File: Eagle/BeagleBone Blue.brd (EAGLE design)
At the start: 86.4 x 54.6 mm, 125 parts, among them M1 JST_ZH_2, M2 JST_ZH_2, M3 JST_ZH_2, M4 JST_ZH_2, Q3 MOSFET-N, Q4 MOSFET-P

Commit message: move Hbridges to back
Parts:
- moved H2 9.46 mm to (81.5, 24.1), flipped to the bottom, turned to 270 degrees
- moved H1 2.01 mm to (74.4, 13.6), flipped to the bottom, turned to 270 degrees
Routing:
- net MOT1B: track 12.2 -> 0.65 mm
- net MOT1A: track 9.95 -> 0.65 mm, vias 1 -> 0
- net MOT2A: track 7.24 -> 0.65 mm
- net MOT2B: track 6.79 -> 0.65 mm
- net GND: track 82.4 -> 81.7 mm

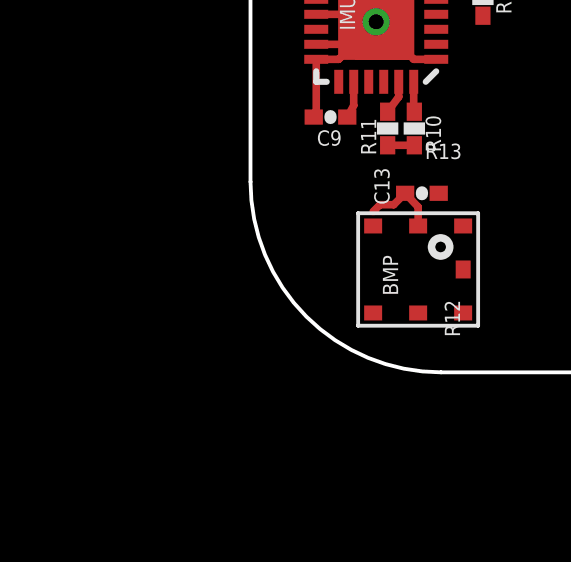
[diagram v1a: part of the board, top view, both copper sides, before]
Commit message: added MPU-9250 component
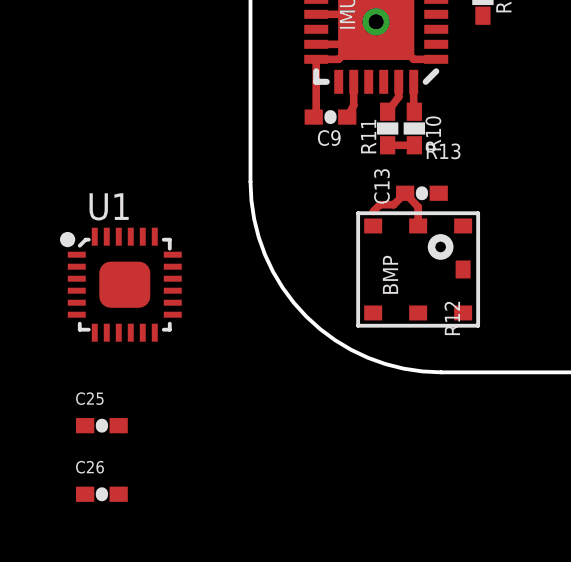
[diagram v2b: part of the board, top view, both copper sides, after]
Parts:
- added C25, C26: 0.1uF, Strawson_Eagle_Lib:0402-CAP
- added U1: MPU-9250, Strawson_Eagle_Lib:QFN24G-0.4-3X3MM
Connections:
- new net N$70: C26.2, U1.10
- net 3.3V: now also C25.1, U1.1, U1.13, U1.8
- net GND: now also C25.2, C26.1, U1.18, U1.20, U1.25, U1.9
- net I2C2_SCL: now also U1.23
- net I2C2_SDA: now also U1.24
- net IMU_INT: now also U1.12
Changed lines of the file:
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@@
 <layer number="56" name="wert" color="7" fill="1" visible="yes" active="yes"/>
 <layer number="57" name="tCAD" color="7" fill="1" visible="no" active="no"/>
+<layer number="90" name="Modules" color="5" fill="1" visible="no" active="no"/>
 <layer number="91" name="Nets" color="2" fill="1" visible="no" active="no"/>
 <layer number="92" name="Busses" color="1" fill="1" visible="no" active="no"/>
@@
 </element>
 <element name="U$7" library="Strawson_Eagle_Lib" package="BEAGLEBONE_BLUE_NO_HOLES" value="" x="0" y="54.61" rot="R270"/>
+<element name="U1" library="Strawson_Eagle_Lib" package="QFN24G-0.4-3X3MM" value="MPU-9250" x="-4.191" y="2.921">
+<attribute name="MPN" value="MPU-9250" x="-4.191" y="2.921" size="1.778" layer="27" display="off"/>
+</element>
+<element name="C25" library="Strawson_Eagle_Lib" package="0402-CAP" value="0.1uF" x="-4.953" y="-1.778"/>
+<element name="C26" library="Strawson_Eagle_Lib" package="0402-CAP" value="0.1uF" x="-4.953" y="-4.064"/>
 </elements>
 <signals>
@@
 <wire x1="4.941" y1="9.684" x2="4.941" y2="9.1828" width="0.254" layer="1"/>
 <wire x1="4.941" y1="9.1828" x2="4.572" y2="8.6868" width="0.254" layer="1"/>
+<contactref element="U1" pad="23"/>
 <wire x1="5.588" y1="1.979" x2="4.572" y2="8.6868" width="0" layer="19" extent="1-1"/>
+<wire x1="-4.791" y1="4.521" x2="4.572" y2="8.6868" width="0" layer="19" extent="1-1"/>
 </signal>
 <signal name="I2C2_SDA">
@@
 <wire x1="5.441" y1="9.684" x2="5.441" y2="8.7068" width="0.254" layer="1"/>
 <wire x1="5.441" y1="8.7068" x2="5.461" y2="8.6868" width="0.254" layer="1"/>
+<contactref element="U1" pad="24"/>
 <wire x1="7.088" y1="1.979" x2="5.461" y2="8.6868" width="0" layer="19" extent="1-1"/>
+<wire x1="-5.191" y1="4.521" x2="5.441" y2="8.7068" width="0" layer="19" extent="1-1"/>
 </signal>
 <signal name="PWM_2B">
@@
 <wire x1="4.7752" y1="5.588" x2="5.1562" y2="5.969" width="0.254" layer="1"/>
 <wire x1="77.0382" y1="41.783" x2="77.0382" y2="40.767" width="0.254" layer="1"/>
-<wire x1="77.0382" y1="41.783" x2="83.28" y2="42.672" width="0" layer="19" extent="1-1"/>
-<wire x1="76.7842" y1="37.084" x2="77.0382" y2="40.767" width="0" layer="19" extent="1-1"/>
-<wire x1="76.7842" y1="36.195" x2="76.7842" y2="37.084" width="0" layer="19" extent="1-1"/>
-<wire x1="77.6478" y1="32.512" x2="76.7842" y2="36.195" width="0" layer="19" extent="1-1"/>
+<contactref element="U1" pad="8"/>
+<contactref element="U1" pad="1"/>
+<contactref element="C25" pad="1"/>
+<contactref element="U1" pad="13"/>
+<wire x1="83.28" y1="37.719" x2="83.28" y2="42.672" width="0" layer="19" extent="1-1"/>
+<wire x1="83.28" y1="32.766" x2="83.28" y2="37.719" width="0" layer="19" extent="1-1"/>
+<wire x1="83.28" y1="27.94" x2="83.28" y2="32.766" width="0" layer="19" extent="1-1"/>
+<wire x1="77.6478" y1="32.512" x2="83.28" y2="32.766" width="0" layer="19" extent="1-1"/>
 <wire x1="76.5302" y1="31.623" x2="77.6478" y2="32.512" width="0" layer="19" extent="1-1"/>
 <wire x1="76.0222" y1="29.21" x2="76.5302" y2="31.623" width="0" layer="19" extent="1-1"/>
 <wire x1="76.0222" y1="28.194" x2="76.0222" y2="29.21" width="0" layer="19" extent="1-1"/>
-<wire x1="83.28" y1="32.766" x2="77.6478" y2="32.512" width="0" layer="19" extent="1-1"/>
-<wire x1="83.28" y1="27.94" x2="83.28" y2="32.766" width="0" layer="19" extent="1-1"/>
-<wire x1="83.28" y1="37.719" x2="83.28" y2="32.766" width="0" layer="19" extent="1-1"/>
-<wire x1="77.878" y1="25.105" x2="76.0222" y2="28.194" width="0" layer="19" extent="1-1"/>
-<wire x1="64.389" y1="18.4658" x2="77.878" y2="25.105" width="0" layer="19" extent="1-1"/>
-<wire x1="70.766" y1="14.564" x2="64.389" y2="18.4658" width="0" layer="19" extent="1-1"/>
-<wire x1="71.247" y1="4.794" x2="70.766" y2="14.564" width="0" layer="19" extent="1-1"/>
+<wire x1="77.878" y1="25.105" x2="76.0222" y2="28.194" width="0" layer="19" extent="1-16"/>
+<wire x1="76.7842" y1="36.195" x2="77.6478" y2="32.512" width="0" layer="19" extent="1-1"/>
+<wire x1="76.7842" y1="37.084" x2="76.7842" y2="36.195" width="0" layer="19" extent="1-1"/>
+<wire x1="77.0382" y1="40.767" x2="76.7842" y2="37.084" width="0" layer="19" extent="1-1"/>
+<wire x1="70.766" y1="14.564" x2="77.878" y2="25.105" width="0" layer="19" extent="16-16"/>
+<wire x1="64.389" y1="18.4658" x2="70.766" y2="14.564" width="0" layer="19" extent="1-16"/>
+<wire x1="71.247" y1="4.794" x2="70.766" y2="14.564" width="0" layer="19" extent="1-16"/>
 <wire x1="64.897" y1="4.921" x2="71.247" y2="4.794" width="0" layer="19" extent="1-1"/>
 <wire x1="53.721" y1="6.413" x2="64.897" y2="4.921" width="0" layer="19" extent="1-1"/>
@@
 <wire x1="28.829" y1="10.0838" x2="34.544" y2="9.9568" width="0" layer="19" extent="1-1"/>
 <wire x1="21.855" y1="6.604" x2="28.829" y2="10.0838" width="0" layer="19" extent="1-1"/>
-<wire x1="5.588" y1="4.879" x2="21.855" y2="6.604" width="0" layer="19" extent="1-1"/>
+<wire x1="5.588" y1="5.5118" x2="21.855" y2="6.604" width="0" layer="19" extent="1-1"/>
 <wire x1="4.088" y1="4.879" x2="4.088" y2="5.358" width="0" layer="19" extent="1-1"/>
 <wire x1="5.461" y1="7.5692" x2="5.1562" y2="5.969" width="0" layer="19" extent="1-1"/>
@@
 <wire x1="6.4008" y1="15.113" x2="4.941" y2="13.684" width="0" layer="19" extent="1-1"/>
 <wire x1="2.191" y1="12.934" x2="4.941" y2="13.684" width="0" layer="19" extent="1-1"/>
+<wire x1="-2.591" y1="1.921" x2="4.088" y2="4.879" width="0" layer="19" extent="1-1"/>
+<wire x1="-4.791" y1="1.321" x2="-2.591" y2="1.921" width="0" layer="19" extent="1-1"/>
+<wire x1="-5.791" y1="3.921" x2="-4.791" y2="1.321" width="0" layer="19" extent="1-1"/>
+<wire x1="-5.5118" y1="-1.778" x2="-4.791" y2="1.321" width="0" layer="19" extent="1-1"/>
 </signal>
 <signal name="N$57">
@@
 <signal name="IMU_INT">
 <contactref element="IMU" pad="12"/>
+<contactref element="U1" pad="12"/>
+<wire x1="-3.191" y1="1.321" x2="2.941" y2="13.684" width="0" layer="19" extent="1-1"/>
 </signal>
 <signal name="QEP_0B">
@@
 <wire x1="46.99" y1="40.132" x2="51.308" y2="40.132" width="0.254" layer="16"/>
 <wire x1="51.308" y1="40.132" x2="51.308" y2="46.101" width="0.254" layer="16"/>
+<contactref element="U1" pad="25"/>
+<contactref element="U1" pad="20"/>
+<contactref element="U1" pad="9"/>
+<contactref element="C25" pad="2"/>
+<contactref element="U1" pad="18"/>
+<contactref element="C26" pad="1"/>
 <wire x1="84.28" y1="37.719" x2="84.28" y2="42.672" width="0" layer="19" extent="1-1"/>
 <wire x1="84.28" y1="32.766" x2="84.28" y2="37.719" width="0" layer="19" extent="1-1"/>
@@
 <wire x1="78.078" y1="11.964" x2="78.078" y2="15.214" width="0" layer="19" extent="16-16"/>
 <wire x1="78.078" y1="11.314" x2="78.078" y2="11.964" width="0" layer="19" extent="16-16"/>
-<wire x1="64.389" y1="17.3482" x2="78.078" y2="15.214" width="0" layer="19" extent="1-16"/>
-<wire x1="70.766" y1="13.264" x2="64.389" y2="17.3482" width="0" layer="19" extent="1-16"/>
-<wire x1="62.738" y1="19.7358" x2="64.389" y2="17.3482" width="0" layer="19" extent="1-1"/>
-<wire x1="71.247" y1="5.794" x2="78.078" y2="11.314" width="0" layer="19" extent="1-16"/>
+<wire x1="70.766" y1="13.264" x2="78.078" y2="11.964" width="0" layer="19" extent="16-16"/>
+<wire x1="71.247" y1="5.794" x2="70.766" y2="13.264" width="0" layer="19" extent="1-16"/>
 <wire x1="64.897" y1="5.921" x2="71.247" y2="5.794" width="0" layer="19" extent="1-1"/>
 <wire x1="58.801" y1="7.413" x2="64.897" y2="5.921" width="0" layer="19" extent="1-1"/>
@@
 <wire x1="30.861" y1="6.175" x2="35.433" y2="6.175" width="0" layer="19" extent="1-1"/>
 <wire x1="30.861" y1="5.175" x2="30.861" y2="6.175" width="0" layer="19" extent="1-1"/>
+<wire x1="64.389" y1="17.3482" x2="70.766" y2="13.264" width="0" layer="19" extent="1-16"/>
+<wire x1="62.738" y1="19.7358" x2="64.389" y2="17.3482" width="0" layer="19" extent="1-1"/>
 <wire x1="63.119" y1="29.197" x2="62.738" y2="19.7358" width="0" layer="19" extent="1-1"/>
 <wire x1="61.087" y1="32.9565" x2="63.119" y2="29.197" width="0" layer="19" extent="1-1"/>
@@
 <wire x1="6.2738" y1="5.969" x2="6.191" y2="10.434" width="0" layer="19" extent="1-1"/>
 <wire x1="7.088" y1="3.429" x2="6.2738" y2="5.969" width="0" layer="19" extent="1-1"/>
+<wire x1="-2.591" y1="3.921" x2="2.1082" y2="8.509" width="0" layer="19" extent="1-1"/>
+<wire x1="-3.591" y1="4.521" x2="-2.591" y2="3.921" width="0" layer="19" extent="1-1"/>
+<wire x1="-4.191" y1="2.921" x2="-3.591" y2="4.521" width="0" layer="19" extent="1-1"/>
+<wire x1="-4.391" y1="1.321" x2="-4.191" y2="2.921" width="0" layer="19" extent="1-1"/>
+<wire x1="-4.3942" y1="-1.778" x2="-4.391" y2="1.321" width="0" layer="19" extent="1-1"/>
+<wire x1="-5.5118" y1="-4.064" x2="-4.3942" y2="-1.778" width="0" layer="19" extent="1-1"/>
 </signal>
 <signal name="BALANCE_PAD">
@@
 <via x="80.645" y="6.35" extent="1-16" drill="3.175"/>
 </signal>
+<signal name="N$70">
+<contactref element="U1" pad="10"/>
+<contactref element="C26" pad="2"/>
+<wire x1="-3.991" y1="1.321" x2="-4.3942" y2="-4.064" width="0" layer="19" extent="1-1"/>
+</signal>
 </signals>
